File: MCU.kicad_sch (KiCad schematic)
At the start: 6 parts, among them U1 STM32G071GBU

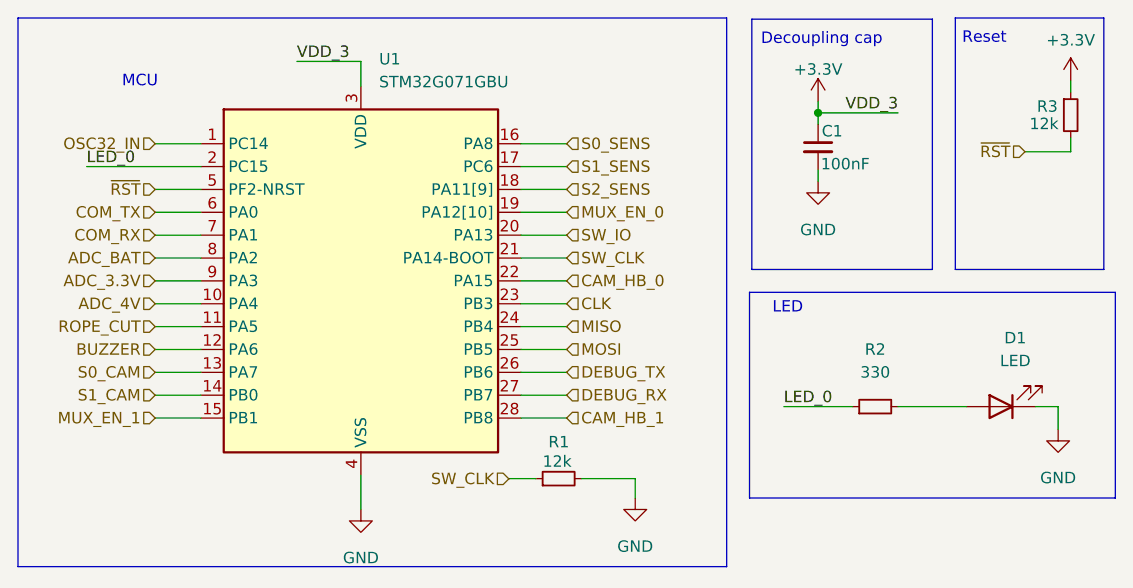
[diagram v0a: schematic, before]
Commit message: 0.3v KiCad
Needs improvements:
-Visual
-Better grounding
-Component placement
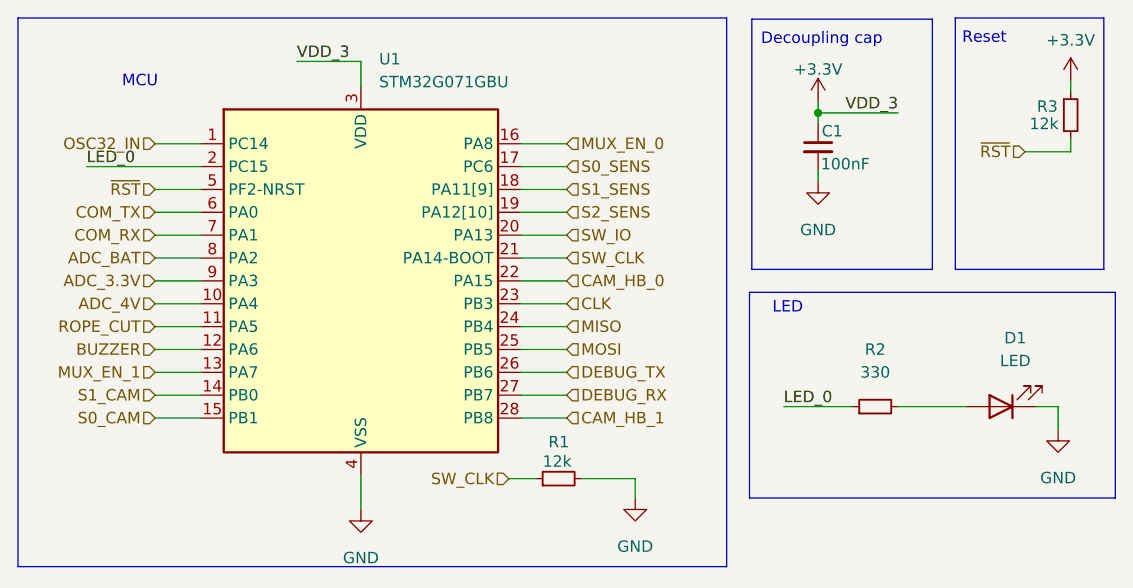
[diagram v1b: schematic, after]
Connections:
- net MUX_EN_0: now also U1.16 (PA8); no longer U1.19 (PA12[10])
- net MUX_EN_1: now also U1.13 (PA7); no longer U1.15 (PB1)
- net S0_CAM: now also U1.15 (PB1); no longer U1.13 (PA7)
- net S0_SENS: now also U1.17 (PC6); no longer U1.16 (PA8)
- net S1_SENS: now also U1.18 (PA11[9]); no longer U1.17 (PC6)
- net S2_SENS: now also U1.19 (PA12[10]); no longer U1.18 (PA11[9])
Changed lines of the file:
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@@
     (effects (font (size 1.27 1.27)) (justify right))
   )
-  (hierarchical_label "S2_SENS" (shape input) (at 76.2 34.29 0)
+  (hierarchical_label "S2_SENS" (shape input) (at 76.2 36.83 0)
     (effects (font (size 1.27 1.27)) (justify left))
   )
@@
     (effects (font (size 1.27 1.27)) (justify left))
   )
-  (hierarchical_label "S1_SENS" (shape input) (at 76.2 31.75 0)
+  (hierarchical_label "S1_SENS" (shape input) (at 76.2 34.29 0)
     (effects (font (size 1.27 1.27)) (justify left))
   )
@@
     (effects (font (size 1.27 1.27)) (justify left))
   )
-  (hierarchical_label "MUX_EN_0" (shape input) (at 76.2 36.83 0)
+  (hierarchical_label "MUX_EN_0" (shape input) (at 76.2 29.21 0)
     (effects (font (size 1.27 1.27)) (justify left))
   )
-  (hierarchical_label "S0_SENS" (shape input) (at 76.2 29.21 0)
+  (hierarchical_label "S0_SENS" (shape input) (at 76.2 31.75 0)
     (effects (font (size 1.27 1.27)) (justify left))
   )
-  (hierarchical_label "S0_CAM" (shape input) (at 30.48 54.61 180)
+  (hierarchical_label "S0_CAM" (shape input) (at 30.48 59.69 180)
     (effects (font (size 1.27 1.27)) (justify right))
   )
@@
     (effects (font (size 1.27 1.27)) (justify left))
   )
-  (hierarchical_label "MUX_EN_1" (shape input) (at 30.48 59.69 180)
+  (hierarchical_label "MUX_EN_1" (shape input) (at 30.48 54.61 180)
     (effects (font (size 1.27 1.27)) (justify right))
   )

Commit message: V1
- Corrected SD-cards footprint and schematical represantation;
- Corrected RTC shematics:
	- changed oscilators power supply from internal 3v3 to Vbat so RTC works when PCB is disconnected from external power supply [PWR PCB];
	- 32 kHz to microcontroller now comes from RTC module;
	- added 100 nF decoupling capacitor to Vbat RTC pin.
- Corrected couple connections and component placement on PCB
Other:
- company: (none) -> BASEMENT
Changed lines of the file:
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@@
 (kicad_sch (version 20211123) (generator eeschema)
   (paper "A4")
+  (title_block
+    (date "%%date%%")
+    (rev "%%version%%")
+    (company "BASEMENT")
+  )
   (junction (at 104.14 25.781) (diameter 0) (color 0 0 0 0)
   )
